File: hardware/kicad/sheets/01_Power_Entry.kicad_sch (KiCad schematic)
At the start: 0 parts

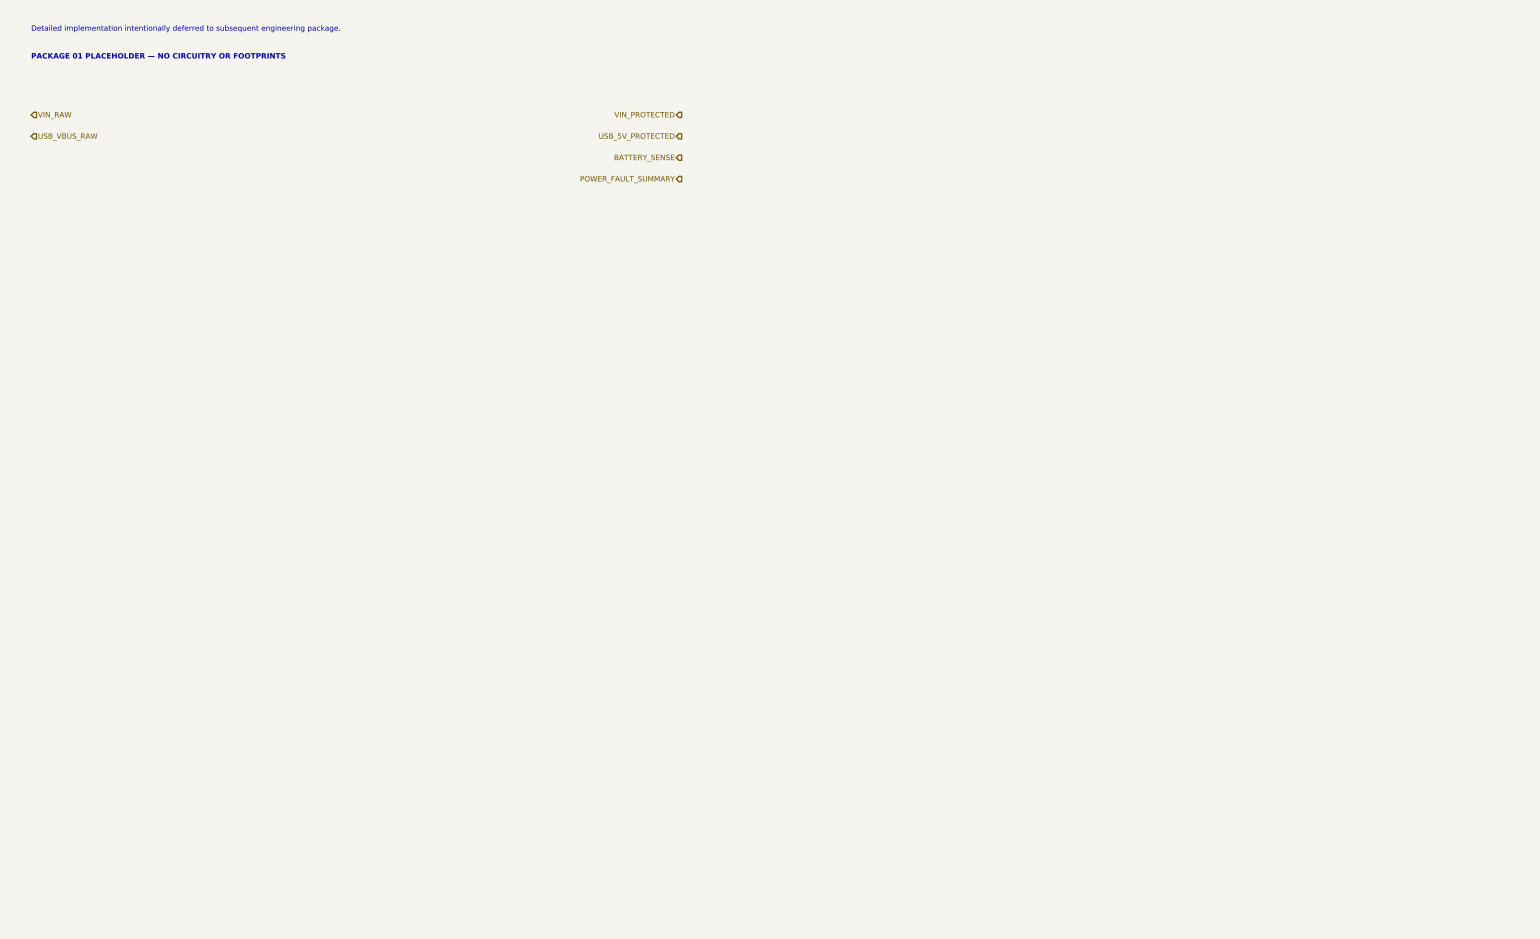
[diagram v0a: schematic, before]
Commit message: Implement Rev A power entry schematic
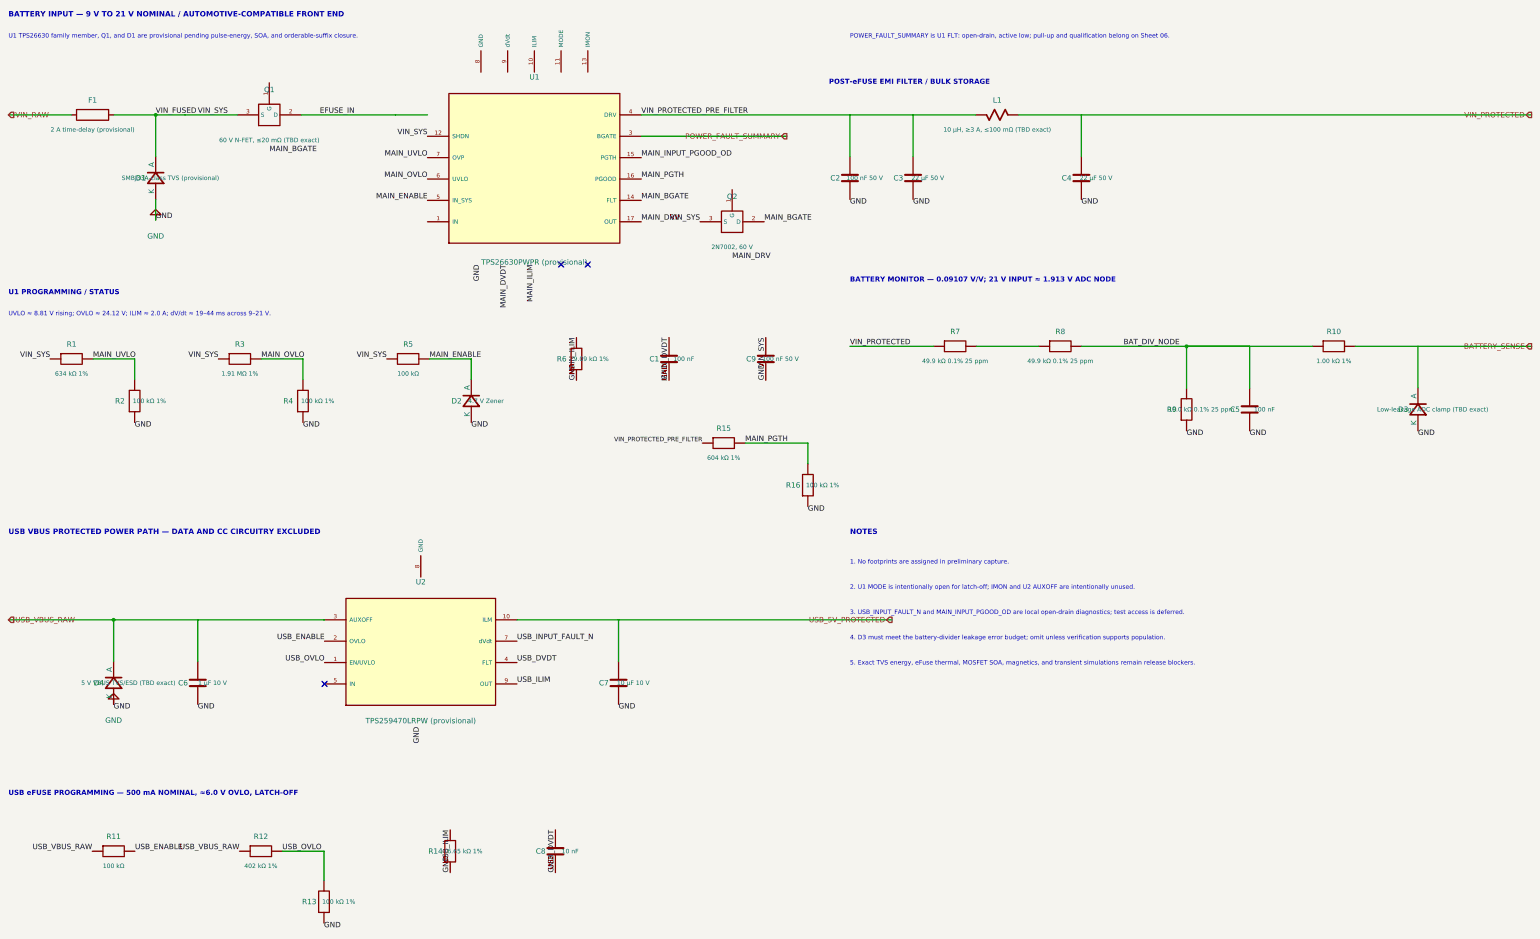
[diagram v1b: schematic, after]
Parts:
- added C1, C5: 100 nF, symbol IPC100:C
- added C2, C9: 100 nF 50 V, symbol IPC100:C
- added C3, C4: 22 µF 50 V, symbol IPC100:C
- added C6: 1 µF 10 V, symbol IPC100:C
- added C7: 10 µF 10 V, symbol IPC100:C
- added C8: 10 nF, symbol IPC100:C
- added D1: SMBJ33A-class TVS (provisional), symbol IPC100:D
- added D2: 4.7 V Zener, symbol IPC100:D
- added D3: Low-leakage ADC clamp (TBD exact), symbol IPC100:D
- added D4: 5 V VBUS TVS/ESD (TBD exact), symbol IPC100:D
- added F1: 2 A time-delay (provisional), symbol IPC100:FUSE
- added L1: 10 µH, ≥3 A, ≤100 mΩ (TBD exact), symbol IPC100:L
- added Q1: 60 V N-FET, ≤20 mΩ (TBD exact), symbol IPC100:NMOS
- added Q2: 2N7002, 60 V, symbol IPC100:NMOS
- added R1: 634 kΩ 1%, symbol IPC100:R
- added R10: 1.00 kΩ 1%, symbol IPC100:R
- added R11, R5: 100 kΩ, symbol IPC100:R
- added R12: 402 kΩ 1%, symbol IPC100:R
- added R13, R16, R2, R4: 100 kΩ 1%, symbol IPC100:R
- added R14: 6.65 kΩ 1%, symbol IPC100:R
- added R15: 604 kΩ 1%, symbol IPC100:R
- added R3: 1.91 MΩ 1%, symbol IPC100:R
- added R6: 9.09 kΩ 1%, symbol IPC100:R
- added R7, R8: 49.9 kΩ 0.1% 25 ppm, symbol IPC100:R
- added R9: 10.0 kΩ 0.1% 25 ppm, symbol IPC100:R
- added U1: TPS26630PWPR (provisional), symbol IPC100:TPS26630
- added U2: TPS259470LRPW (provisional), symbol IPC100:TPS259470L
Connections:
- net BATTERY_SENSE: now also R10.2
- net POWER_FAULT_SUMMARY: now also U1.3 (BGATE)
- net USB_5V_PROTECTED: now also U2.10 (ILM)
- net USB_VBUS_RAW: now also D4.2 (A), R11.1, R12.1, U2.3 (AUXOFF)
- net VIN_PROTECTED: now also L1.2, R7.1
- net VIN_RAW: now also F1.1
- new net: R7.2, R8.1
- new net BAT_DIV_NODE: C5.2, R10.1, R8.2, R9.2
- new net EFUSE_IN: Q1.2 (D)
- new net GND: C1.1, C2.1, C3.1, C4.1, C5.1, C6.1, C7.1, C8.1, C9.1, D1.1 (K), D2.1 (K), D3.1 (K), D4.1 (K), R13.1, R14.1, R16.1, R2.1, R4.1, R6.1, R9.1
- new net MAIN_BGATE: Q2.2 (D), U1.14 (FLT)
- new net MAIN_DRV: U1.17 (OUT)
- new net MAIN_DVDT: C1.2
- new net MAIN_ENABLE: D2.2 (A), R5.2, U1.5 (IN_SYS)
- new net MAIN_ILIM: R6.2
- new net MAIN_INPUT_PGOOD_OD: U1.15 (PGTH)
- new net MAIN_OVLO: R3.2, R4.2, U1.6 (UVLO)
- new net MAIN_PGTH: R15.2, R16.2, U1.16 (PGOOD)
- new net MAIN_UVLO: R1.2, R2.2, U1.7 (OVP)
- new net USB_DVDT: C8.2, U2.4 (FLT)
- new net USB_ENABLE: R11.2, U2.2 (OVLO)
- new net USB_ILIM: R14.2, U2.9 (OUT)
- new net USB_INPUT_FAULT_N: U2.7 (dVdt)
- new net USB_OVLO: R12.2, R13.2, U2.1 (EN/UVLO)
- new net VIN_FUSED: C9.2, D1.2 (A), F1.2, Q1.3 (S), Q2.3 (S), R1.1, R3.1, R5.1, U1.12 (SHDN)
- new net VIN_PROTECTED_PRE_FILTER: C3.2, L1.1, R15.1, U1.4 (DRV)
- no-connect marks 0 -> 3
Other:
- note added: "1. No footprints are assigned in preliminary capture."
- note added: "2. U1 MODE is intentionally open for latch-off; IMON and U2 AUXOFF are intentionally unused."
- note added: "3. USB_INPUT_FAULT_N and MAIN_INPUT_PGOOD_OD are local open-drain diagnostics; test access is deferred."
- note added: "4. D3 must meet the battery-divider leakage error budget; omit unless verification supports population."
- note added: "5. Exact TVS energy, eFuse thermal, MOSFET SOA, magnetics, and transient simulations remain release blockers."
- note added: "BATTERY INPUT — 9 V TO 21 V NOMINAL / AUTOMOTIVE-COMPATIBLE FRONT END"
- note added: "BATTERY MONITOR — 0.09107 V/V; 21 V INPUT ≈ 1.913 V ADC NODE"
- note added: "NOTES"
- note added: "POST-eFUSE EMI FILTER / BULK STORAGE"
- note added: "POWER_FAULT_SUMMARY is U1 FLT: open-drain, active low; pull-up and qualification belong on Sheet 06."
- note added: "U1 PROGRAMMING / STATUS"
- note added: "U1 TPS26630 family member, Q1, and D1 are provisional pending pulse-energy, SOA, and orderable-suffix closure."
- note added: "USB VBUS PROTECTED POWER PATH — DATA AND CC CIRCUITRY EXCLUDED"
- note added: "USB eFUSE PROGRAMMING — 500 mA NOMINAL, ≈6.0 V OVLO, LATCH-OFF"
- note added: "UVLO ≈ 8.81 V rising; OVLO ≈ 24.12 V; ILIM ≈ 2.0 A; dV/dt ≈ 19–44 ms across 9–21 V."
- note removed: "Detailed implementation intentionally deferred to subsequent engineering package."
- note removed: "PACKAGE 01 PLACEHOLDER — NO CIRCUITRY OR FOOTPRINTS"

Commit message: Resolve Rev A power control interfaces
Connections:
- net MAIN_INPUT_PGOOD_OD renamed MAIN_INPUT_VALID
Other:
- note added: "3. MAIN_INPUT_VALID is released-valid open-drain; Sheet 02 owns main-domain bias and qualification."
- note removed: "3. USB_INPUT_FAULT_N and MAIN_INPUT_PGOOD_OD are local open-drain diagnostics; test access is deferred."
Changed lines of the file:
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@@
     (effects (font (size 1.27 1.27)) (justify right)))
   (wire (pts (xy 170.4 50.08) (xy 205 50.08)) (stroke (width 0) (type default)))
-  (label "MAIN_INPUT_PGOOD_OD" (at 170.4 55.16 0) (effects (font (size 1.27 1.27)) (justify left bottom)))
+  (wire (pts (xy 170.4 55.16) (xy 205 55.16)) (stroke (width 0) (type default)))
+  (hierarchical_label "MAIN_INPUT_VALID" (shape output) (at 205 55.16 180)
+    (effects (font (size 1.27 1.27)) (justify right)))
   (label "MAIN_PGTH" (at 170.4 60.24 0) (effects (font (size 1.27 1.27)) (justify left bottom)))
   (label "GND" (at 132.3 80.56 90) (effects (font (size 1.27 1.27)) (justify right bottom)))
@@
   (text "1. No footprints are assigned in preliminary capture." (at 220 152 0) (effects (font (size 1.05 1.05)) (justify left bottom)))
   (text "2. U1 MODE is intentionally open for latch-off; IMON and U2 AUXOFF are intentionally unused." (at 220 158 0) (effects (font (size 1.05 1.05)) (justify left bottom)))
-  (text "3. USB_INPUT_FAULT_N and MAIN_INPUT_PGOOD_OD are local open-drain diagnostics; test access is deferred." (at 220 164 0) (effects (font (size 1.05 1.05)) (justify left bottom)))
+  (text "3. MAIN_INPUT_VALID is released-valid open-drain; Sheet 02 owns main-domain bias and qualification." (at 220 164 0) (effects (font (size 1.05 1.05)) (justify left bottom)))
   (text "4. D3 must meet the battery-divider leakage error budget; omit unless verification supports population." (at 220 170 0) (effects (font (size 1.05 1.05)) (justify left bottom)))
   (text "5. Exact TVS energy, eFuse thermal, MOSFET SOA, magnetics, and transient simulations remain release blockers." (at 220 176 0) (effects (font (size 1.05 1.05)) (justify left bottom)))

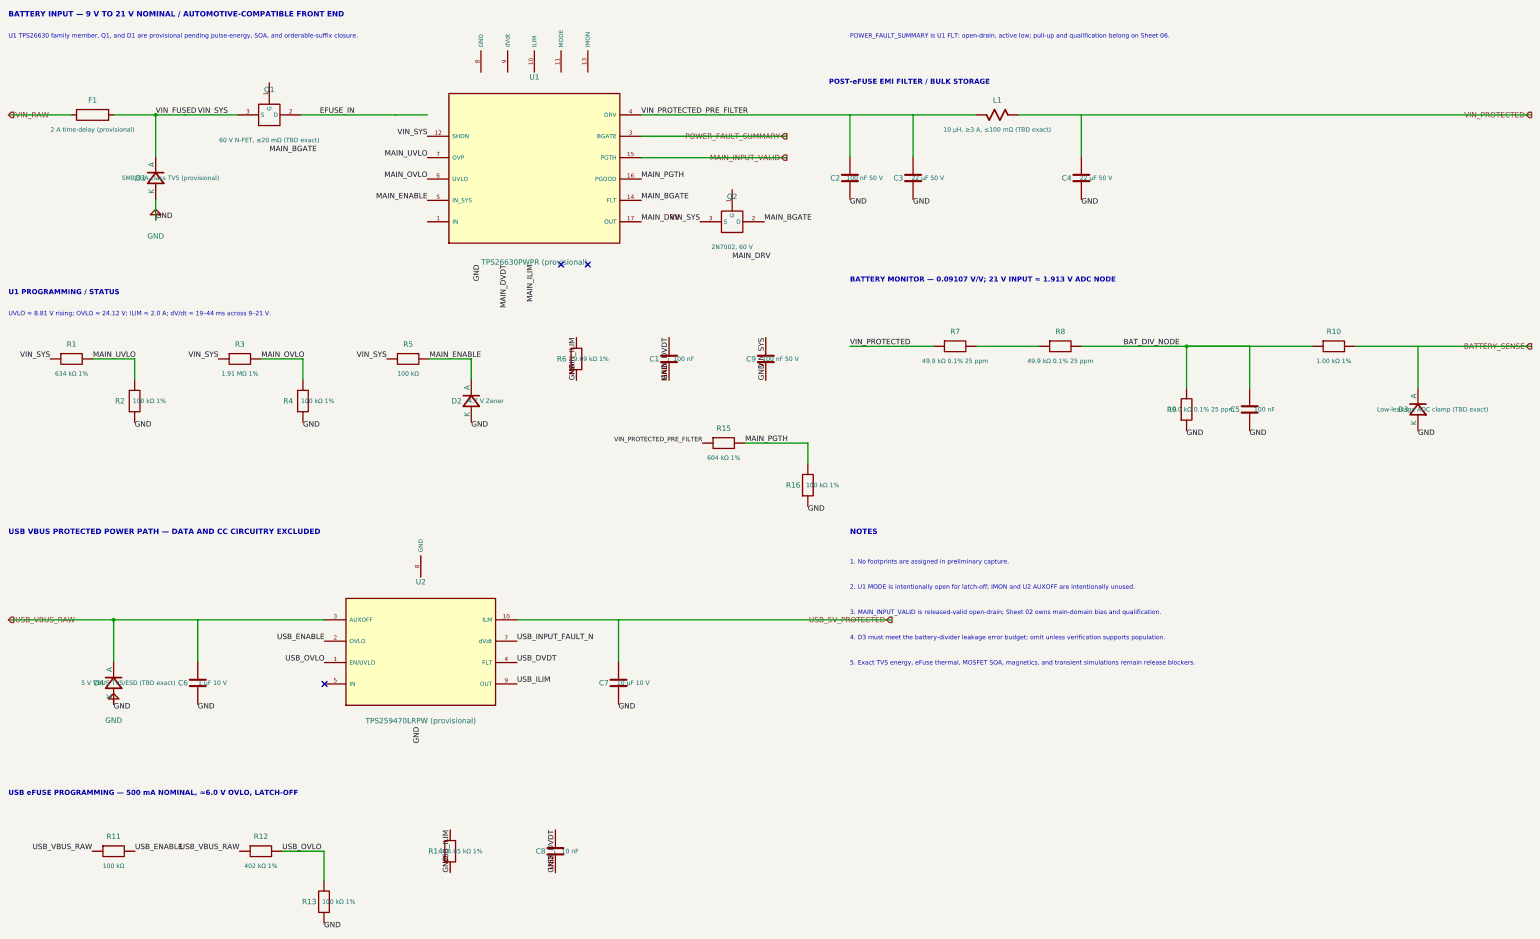
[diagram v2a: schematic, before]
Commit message: Normalize Rev A reference designators
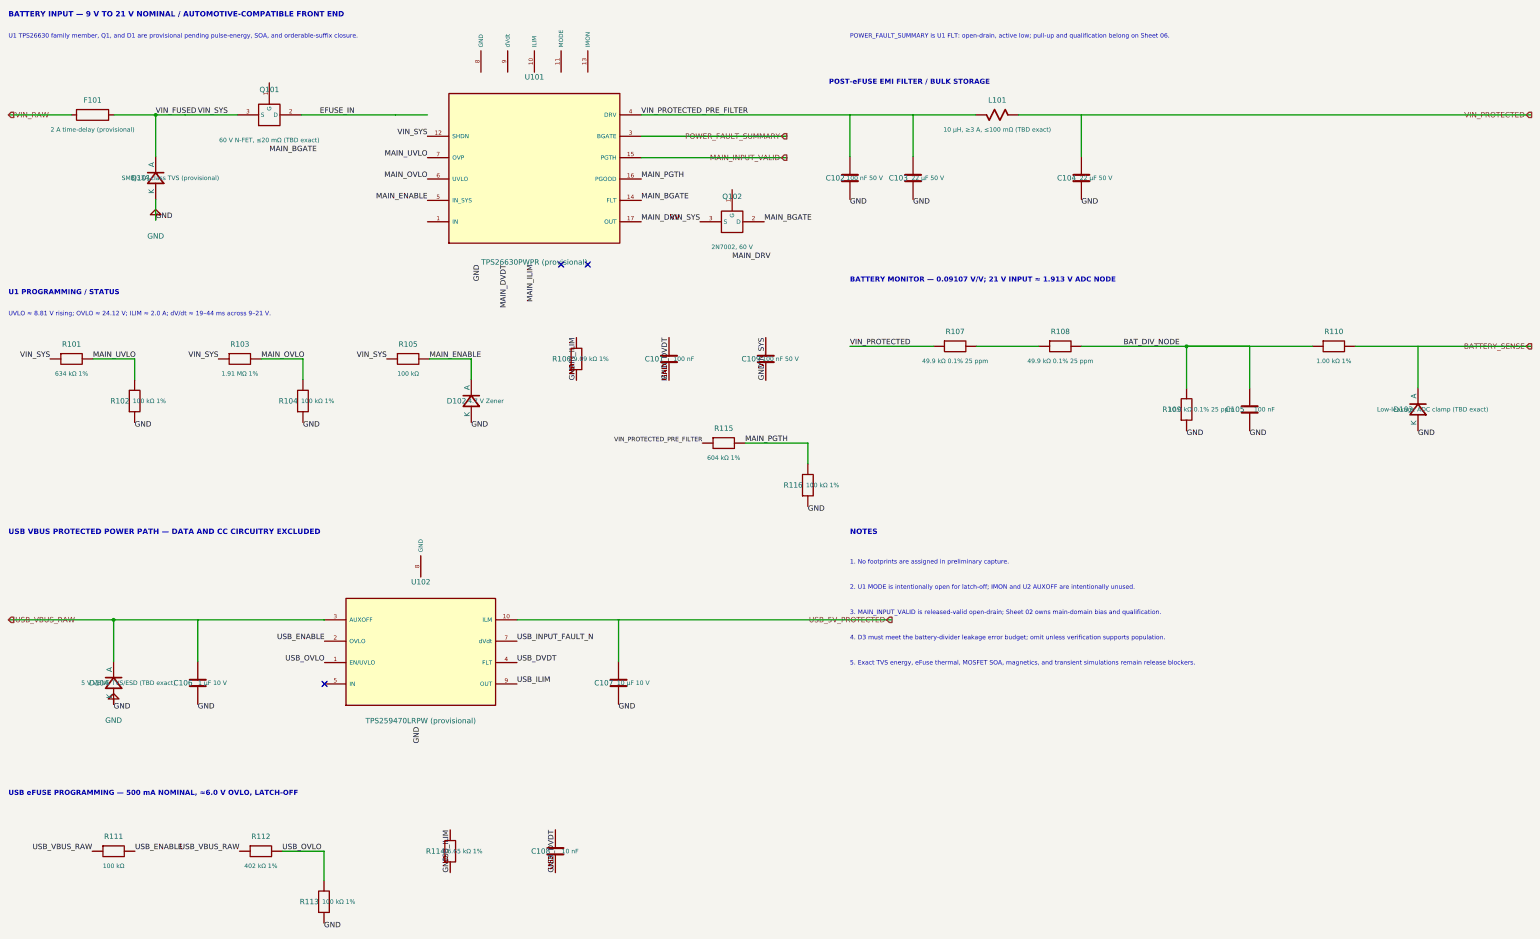
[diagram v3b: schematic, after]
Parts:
- renumbered C1 to C101, C2 to C102, C3 to C103, C4 to C104, C5 to C105, C6 to C106, C7 to C107, C8 to C108, C9 to C109, D1 to D101, D2 to D102, D3 to D103, D4 to D104, F1 to F101, L1 to L101, Q1 to Q101, Q2 to Q102, R1 to R101, R2 to R102, R3 to R103, R4 to R104, R5 to R105, R6 to R106, R7 to R107, R8 to R108, R9 to R109, R10 to R110, R11 to R111, R12 to R112, R13 to R113, R14 to R114, R15 to R115, R16 to R116, U1 to U101, U2 to U102
